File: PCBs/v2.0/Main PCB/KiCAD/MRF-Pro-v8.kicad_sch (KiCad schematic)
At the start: 4 parts, among them J1 Feather-1, J2 Feather-2, J3 FPC 8P Connector, J4 Conn_01x08

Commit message: Switch connectors to in-stock parts and fix the 0-ohm jumper
Align the JST-SH connectors to the established v1/README parts instead
of genuine-JST Extended ones: J4 8-pin C7430450 (the main-board J4 had
a 6-pin number, C7430448, by mistake), J7 6-pin C7430448, J6 4-pin
C7430446. Swap FB1 to C17477 - the prior C2889442 was out of stock and
Extended; C17477 is Basic and well-stocked. Applied across schematic,
footprint fields, and the JLCPCB BOM on both boards.
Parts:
- J4: LCSC C7430448 -> C7430450
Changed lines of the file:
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@@
 			)
 		)
-		(property "LCSC" "C7430448"
+		(property "LCSC" "C7430450"
 			(at 104.14 49.53 90)
 			(hide yes)

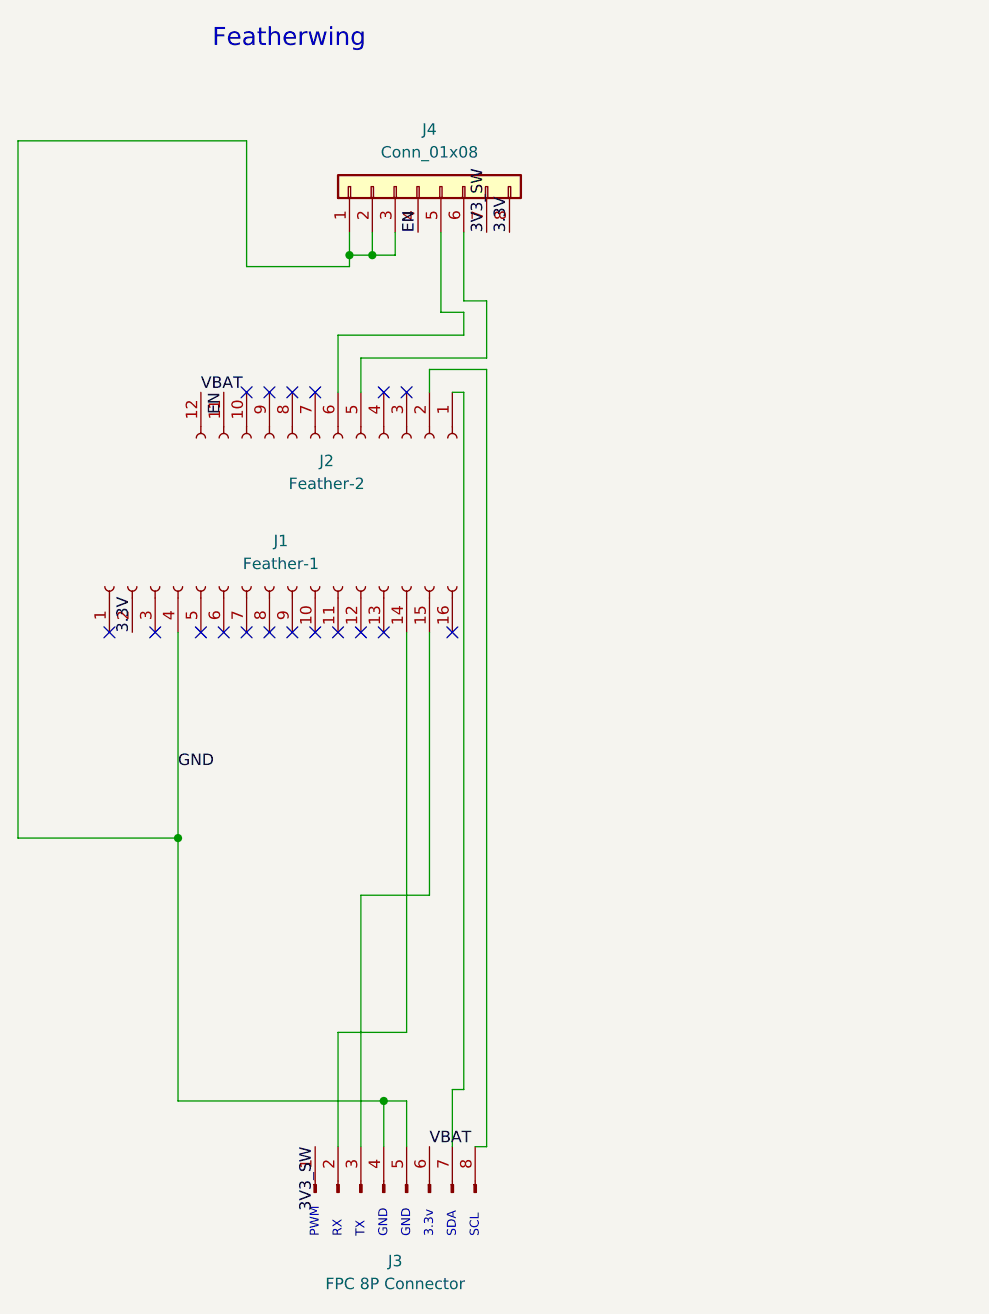
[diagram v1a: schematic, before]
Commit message: Swap FPC pins 1 and 6, reroute both boards, re-plot fab
VBAT now lands on FPC pin 1 (beside the UART pair) and the switched 3.3 V
on pin 6 (beside the I2C pair), so the always-on battery rail no longer
runs next to the I2C lines. Both boards' schematics were tidied up and
fully rerouted; DRC passes clean on each. Gerbers and the JLCPCB position
files are re-plotted to match. The BOM is unchanged - this is a net and
placement change, not a parts change.
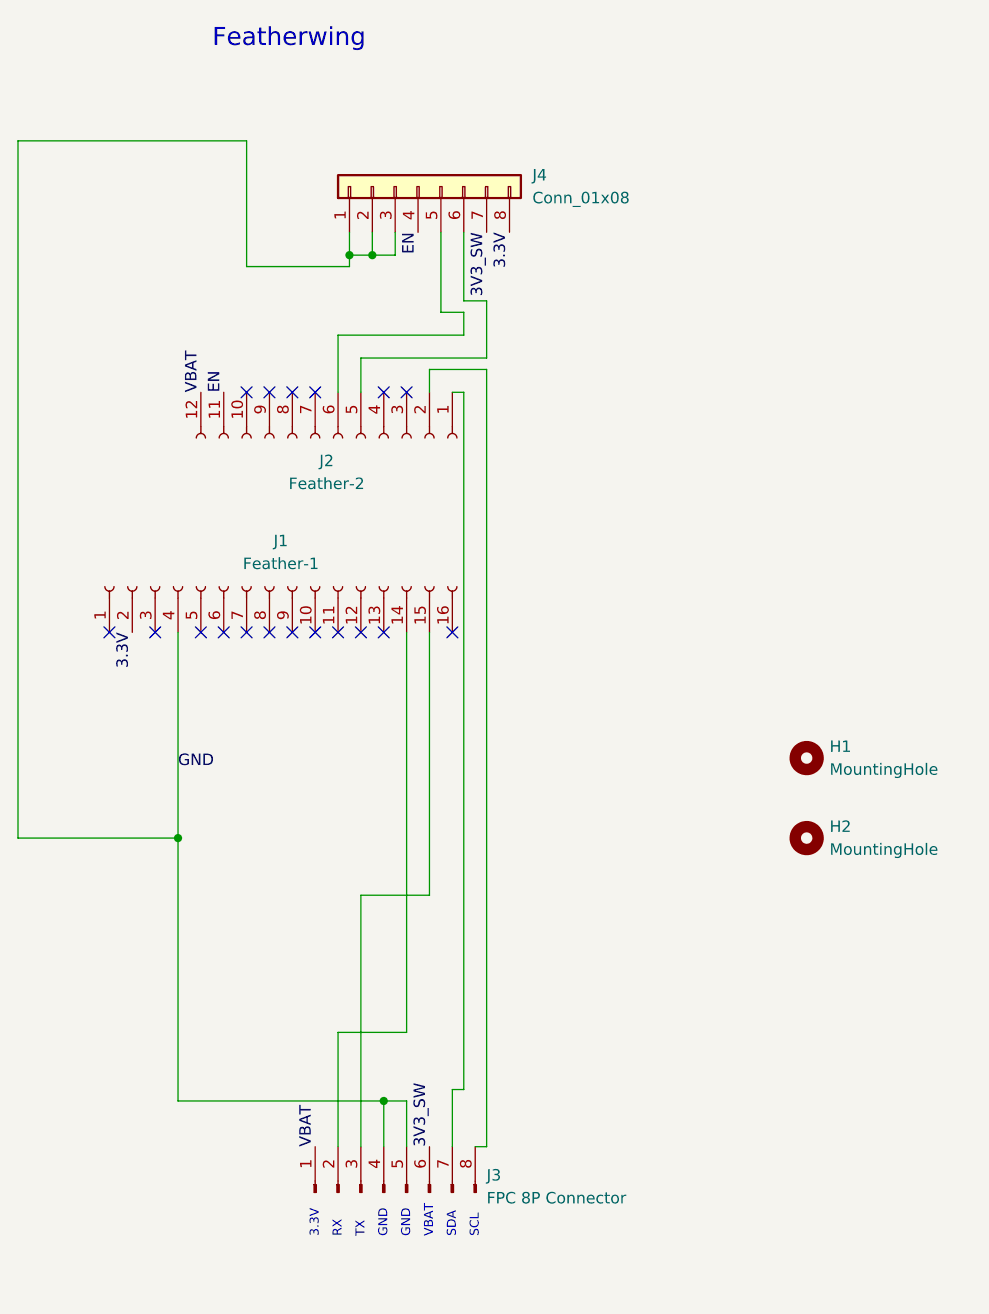
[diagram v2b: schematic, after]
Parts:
- added H1, H2: MountingHole, MountingHole:MountingHole_2.2mm_M2, symbol Mechanical:MountingHole
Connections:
- net 3V3_SW: now also J3.6 (Pin_6); no longer J3.1 (Pin_1)
- net VBAT: now also J3.1 (Pin_1); no longer J3.6 (Pin_6)
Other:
- note added: "3.3V"
- note added: "VBAT"
- note removed: "3.3v"
- note removed: "PWM"
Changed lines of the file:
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@@
 		)
 	)
-	(text "PWM"
+	(text "3.3V"
 		(exclude_from_sim no)
 		(at 93.218 166.37 90)
@@
 		)
 	)
-	(text "3.3v"
+	(text "VBAT"
 		(exclude_from_sim no)
 		(at 105.918 166.37 90)
@@
 		)
 	)
+	(label "3V3_SW"
+		(at 105.41 156.21 90)
+		(effects
+			(font
+				(size 1.27 1.27)
+			)
+			(justify left bottom)
+		)
+	)
 	(label "GND"
 		(at 77.47 114.3 0)
@@
 		(property "Net Class" "GND"
 			(at 77.47 115.57 0)
+			(hide yes)
 			(show_name no)
 			(do_not_autoplace no)
@@
 		)
 	)
+	(label "3.3V"
+		(at 72.39 99.06 270)
+		(effects
+			(font
+				(size 1.27 1.27)
+			)
+			(justify right bottom)
+		)
+	)
 	(label "VBAT"
-		(at 105.41 156.21 0)
+		(at 92.71 156.21 90)
 		(effects
 			(font
@@
 		)
 	)
+	(label "VBAT"
+		(at 80.01 72.39 90)
+		(effects
+			(font
+				(size 1.27 1.27)
+			)
+			(justify left bottom)
+		)
+	)
+	(label "EN"
+		(at 104.14 54.61 270)
+		(effects
+			(font
+				(size 1.27 1.27)
+			)
+			(justify right bottom)
+		)
+	)
+	(label "EN"
+		(at 82.55 72.39 90)
+		(effects
+			(font
+				(size 1.27 1.27)
+			)
+			(justify left bottom)
+		)
+	)
 	(label "3V3_SW"
-		(at 92.71 156.21 270)
+		(at 111.76 54.61 270)
 		(effects
 			(font
@@
 	)
 	(label "3.3V"
-		(at 72.39 99.06 90)
+		(at 114.3 54.61 270)
 		(effects
 			(font
 				(size 1.27 1.27)
 			)
-			(justify left bottom)
-		)
-	)
-	(label "VBAT"
-		(at 80.01 72.39 0)
-		(effects
-			(font
-				(size 1.27 1.27)
-			)
-			(justify left bottom)
-		)
-	)
-	(label "EN"
-		(at 104.14 54.61 90)
-		(effects
-			(font
-				(size 1.27 1.27)
-			)
-			(justify left bottom)
-		)
-	)
-	(label "EN"
-		(at 82.55 72.39 270)
-		(effects
-			(font
-				(size 1.27 1.27)
-			)
 			(justify right bottom)
 		)
 	)
-	(label "3V3_SW"
-		(at 111.76 54.61 90)
-		(effects
-			(font
-				(size 1.27 1.27)
-			)
-			(justify left bottom)
-		)
-	)
-	(label "3.3V"
-		(at 114.3 54.61 90)
-		(effects
-			(font
-				(size 1.27 1.27)
-			)
-			(justify left bottom)
+	(symbol
+		(lib_id "Mechanical:MountingHole")
+		(at 147.32 113.03 0)
+		(unit 1)
+		(body_style 1)
+		(exclude_from_sim no)
+		(in_bom no)
+		(on_board yes)
+		(in_pos_files yes)
+		(dnp no)
+		(fields_autoplaced yes)
+		(property "Reference" "H1"
+			(at 149.86 111.7599 0)
+			(show_name no)
+			(do_not_autoplace no)
+			(effects
+				(font
+					(size 1.27 1.27)
+				)
+				(justify left)
+			)
+		)
+		(property "Value" "MountingHole"
+			(at 149.86 114.2999 0)
+			(show_name no)
+			(do_not_autoplace no)
+			(effects
+				(font
+					(size 1.27 1.27)
+				)
+				(justify left)
+			)
+		)
+		(property "Footprint" "MountingHole:MountingHole_2.2mm_M2"
+			(at 147.32 113.03 0)
+			(hide yes)
+			(show_name no)
+			(do_not_autoplace no)
+			(effects
+				(font
+					(size 1.27 1.27)
+				)
+			)
+		)
+		(property "Datasheet" ""
+			(at 147.32 113.03 0)
+			(hide yes)
+			(show_name no)
+			(do_not_autoplace no)
+			(effects
+				(font
+					(size 1.27 1.27)
+				)
+			)
+		)
+		(property "Description" "Mounting Hole without connection"
+			(at 147.32 113.03 0)
+			(hide yes)
+			(show_name no)
+			(do_not_autoplace no)
+			(effects
+				(font
+					(size 1.27 1.27)
+				)
+			)
+		)
+		(instances
+			(project "MRF-Pro-v8"
+				(path "/896eaae8-6acf-41d9-a1f7-3a80349c3bd9"
+					(reference "H1")
+					(unit 1)
+				)
+			)
 		)
 	)
@@
 		(in_pos_files yes)
 		(dnp no)
+		(fields_autoplaced yes)
 		(property "Reference" "J3"
-			(at 101.6 168.91 90)
-			(show_name no)
-			(do_not_autoplace no)
-			(effects
-				(font
-					(size 1.27 1.27)
-				)
+			(at 111.76 159.3849 90)
+			(show_name no)
+			(do_not_autoplace no)
+			(effects
+				(font
+					(size 1.27 1.27)
+				)
+				(justify right)
 			)
 		)
 		(property "Value" "FPC 8P Connector"
-			(at 101.6 171.45 90)
-			(show_name no)
-			(do_not_autoplace no)
-			(effects
-				(font
-					(size 1.27 1.27)
-				)
+			(at 111.76 161.9249 90)
+			(show_name no)
+			(do_not_autoplace no)
+			(effects
+				(font
+					(size 1.27 1.27)
+				)
+				(justify right)
 			)
 		)
@@
 		(fields_autoplaced yes)
 		(property "Reference" "J4"
-			(at 105.41 43.18 90)
-			(show_name no)
-			(do_not_autoplace no)
-			(effects
-				(font
-					(size 1.27 1.27)
-				)
+			(at 116.84 48.2599 90)
+			(show_name no)
+			(do_not_autoplace no)
+			(effects
+				(font
+					(size 1.27 1.27)
+				)
+				(justify right)
 			)
 		)
 		(property "Value" "Conn_01x08"
-			(at 105.41 45.72 90)
-			(show_name no)
-			(do_not_autoplace no)
-			(effects
-				(font
-					(size 1.27 1.27)
-				)
+			(at 116.84 50.7999 90)
+			(show_name no)
+			(do_not_autoplace no)
+			(effects
+				(font
+					(size 1.27 1.27)
+				)
+				(justify right)
 			)
 		)
@@
 					(unit 1)
 				)
+			)
+		)
+	)
+	(symbol
+		(lib_id "Mechanical:MountingHole")
+		(at 147.32 121.92 0)
+		(unit 1)
+		(body_style 1)
+		(exclude_from_sim no)
+		(in_bom no)
+		(on_board yes)
+		(in_pos_files yes)
+		(dnp no)
+		(fields_autoplaced yes)
+		(property "Reference" "H2"
+			(at 149.86 120.6499 0)
+			(show_name no)
+			(do_not_autoplace no)
+			(effects
+				(font
+					(size 1.27 1.27)
+				)
+				(justify left)
+			)
+		)
+		(property "Value" "MountingHole"
+			(at 149.86 123.1899 0)
+			(show_name no)
+			(do_not_autoplace no)
+			(effects
+				(font
+					(size 1.27 1.27)
+				)
+				(justify left)
+			)
+		)
+		(property "Footprint" "MountingHole:MountingHole_2.2mm_M2"
+			(at 147.32 121.92 0)
+			(hide yes)
+			(show_name no)
+			(do_not_autoplace no)
+			(effects
+				(font
+					(size 1.27 1.27)
+				)
+			)
+		)
+		(property "Datasheet" ""
+			(at 147.32 121.92 0)
+			(hide yes)
+			(show_name no)
+			(do_not_autoplace no)
+			(effects
+				(font
+					(size 1.27 1.27)
+				)
+			)
+		)
+		(property "Description" "Mounting Hole without connection"
+			(at 147.32 121.92 0)
+			(hide yes)
+			(show_name no)
+			(do_not_autoplace no)
+			(effects
+				(font
+					(size 1.27 1.27)
+				)
+			)
+		)
+		(instances
+			(project "MRF-Pro-v8"
+				(path "/896eaae8-6acf-41d9-a1f7-3a80349c3bd9"
+					(reference "H2")
+					(unit 1)
+				)

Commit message: MRF-Pro-v8: rework main-board power-switch nets and re-plot fab
The J4 DPDT power-switch nets were local labels named 3.3V and 3V3_SW,
which didn't read clearly and left the routing awkward. Rename them to
3.3IN (Feather 3.3 V into pole A) and 3.3OUT (switched 3.3 V out to FPC
pin 6) and make them global labels so the net role is obvious on the
sheet. Drop the now-redundant /3.3V and /GND netclass assignments,
reroute to match, and refill the pours. DRC clean: 0 violations, 0
unconnected. The breakout sheet is untouched, so its 3.3V net keeps its
name (3.3OUT on the main board = 3.3V on the breakout, joined by the FPC).

Footprint placement is unchanged, so the JLCPCB BOM and positions stay
valid. Re-plot the main-board Gerbers and drill from the reworked layout.

Sync the hardware-errata docs and the J4 diagram to the new net names,
and mark the Stage-2 LDO errata as layout-done / fab-plotted.
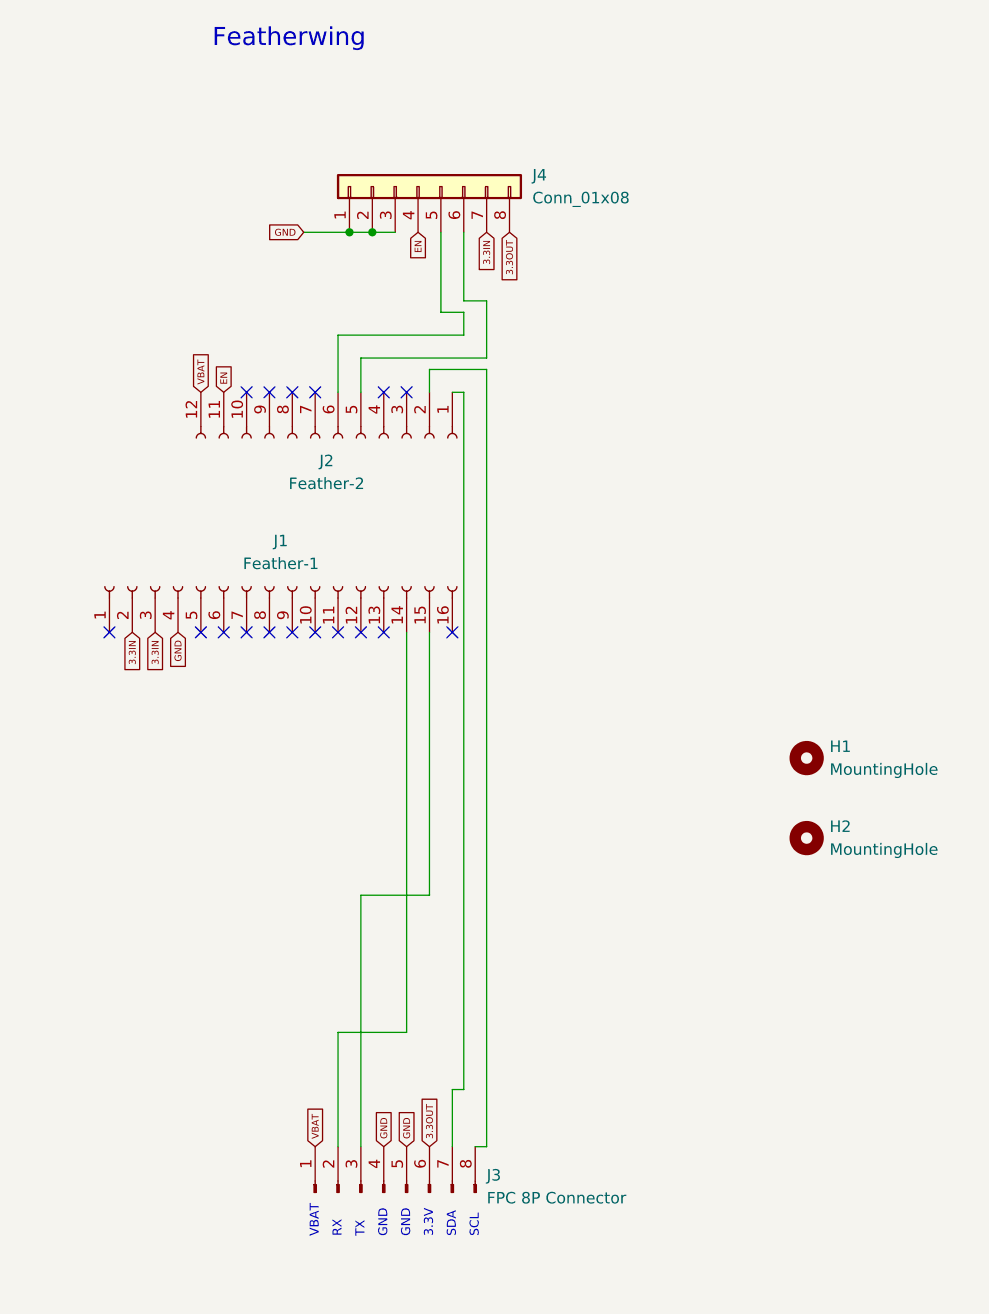
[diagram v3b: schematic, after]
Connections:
- net 3.3IN: now reaches J1.3 (Pin_3)
- net 3.3IN: now also J1.2 (Pin_2), J4.7 (Pin_7)
- net 3.3V renamed 3.3OUT
- net 3.3OUT: now also J3.6 (Pin_6); no longer J1.2 (Pin_2)
- removed net 3V3_SW: J3.6 (Pin_6), J4.7 (Pin_7)
- no-connect marks 18 -> 17
